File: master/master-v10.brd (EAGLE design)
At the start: 48.3 x 59.7 mm, 42 parts, among them IC2 DS3231/SO, J1 AVR_SPI_PRG_6PTH, J2 TWIG-2.0-DIPD, J3 TWIG-2.0-DIPD, J4 TWIG-2.0-DIPD, U1 MCP9804, U2 ATMEGA640/1280/2560-A, U3 FT232RL-BASICSSOP, U4 AP1117E, U5 USD-SOCKETNEW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

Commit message: agregados pads
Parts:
- added V_IN, V_OUT: MOUNT-PAD-ROUND3.0, holes:3,0-PAD
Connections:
- net VIN+: now also V_IN.B3,0
- net VIN-: now also V_OUT.B3,0
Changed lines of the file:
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@@
 <attribute name="SKU" value="PRT-09914" x="8.89" y="6.35" size="1.778" layer="27" font="vector" ratio="15" rot="R180" display="off"/>
 </element>
+<element name="V_OUT" library="holes" package="3,0-PAD" value="MOUNT-PAD-ROUND3.0" x="-124.46" y="-48.26"/>
+<element name="V_IN" library="holes" package="3,0-PAD" value="MOUNT-PAD-ROUND3.0" x="-133.35" y="-48.26"/>
 </elements>
 <signals>
@@
 <contactref element="R12" pad="2"/>
 <contactref element="U6" pad="3"/>
+<contactref element="V_IN" pad="B3,0"/>
+<wire x1="-100.65" y1="-1.3001" x2="-133.35" y2="-48.26" width="0" layer="19" extent="1-1"/>
 <wire x1="-63.37" y1="63.5" x2="-100.65" y2="-1.3001" width="0" layer="19" extent="1-1"/>
 </signal>
@@
 <contactref element="R12" pad="1"/>
 <contactref element="U6" pad="4"/>
+<contactref element="V_OUT" pad="B3,0"/>
+<wire x1="-100.65" y1="1.3001" x2="-124.46" y2="-48.26" width="0" layer="19" extent="1-1"/>
 <wire x1="-66.17" y1="63.5" x2="-100.65" y2="1.3001" width="0" layer="19" extent="1-1"/>
 </signal>

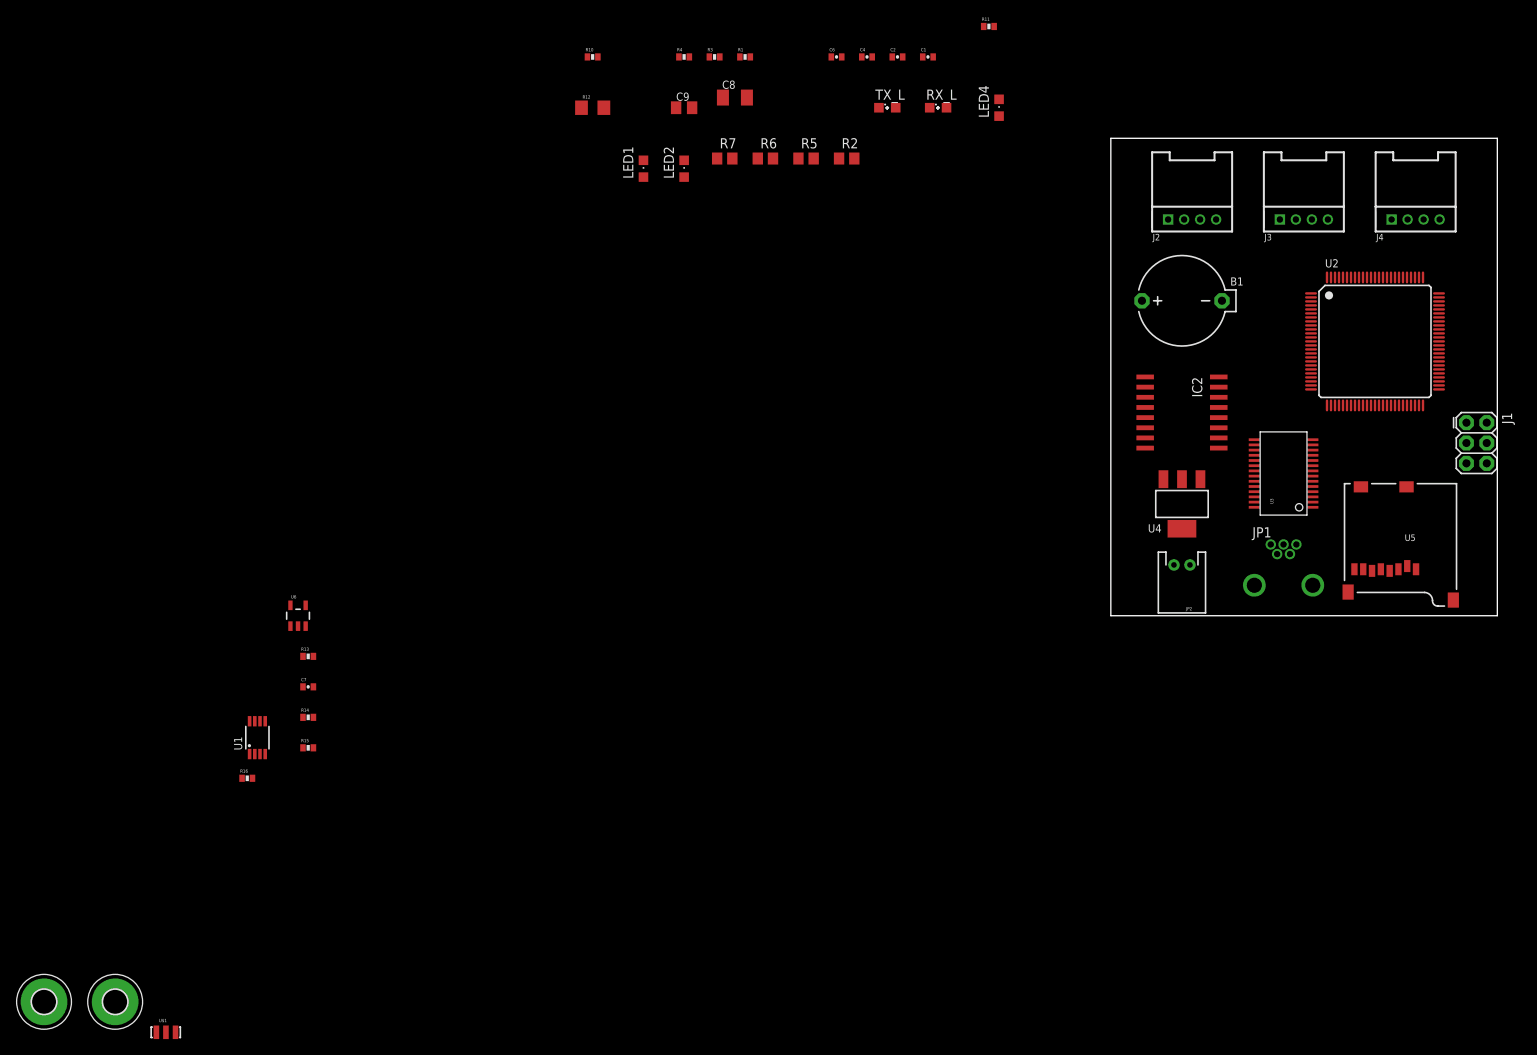
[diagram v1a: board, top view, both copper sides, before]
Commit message: actualizado brd, y arreglado tamaño de algunos componentes
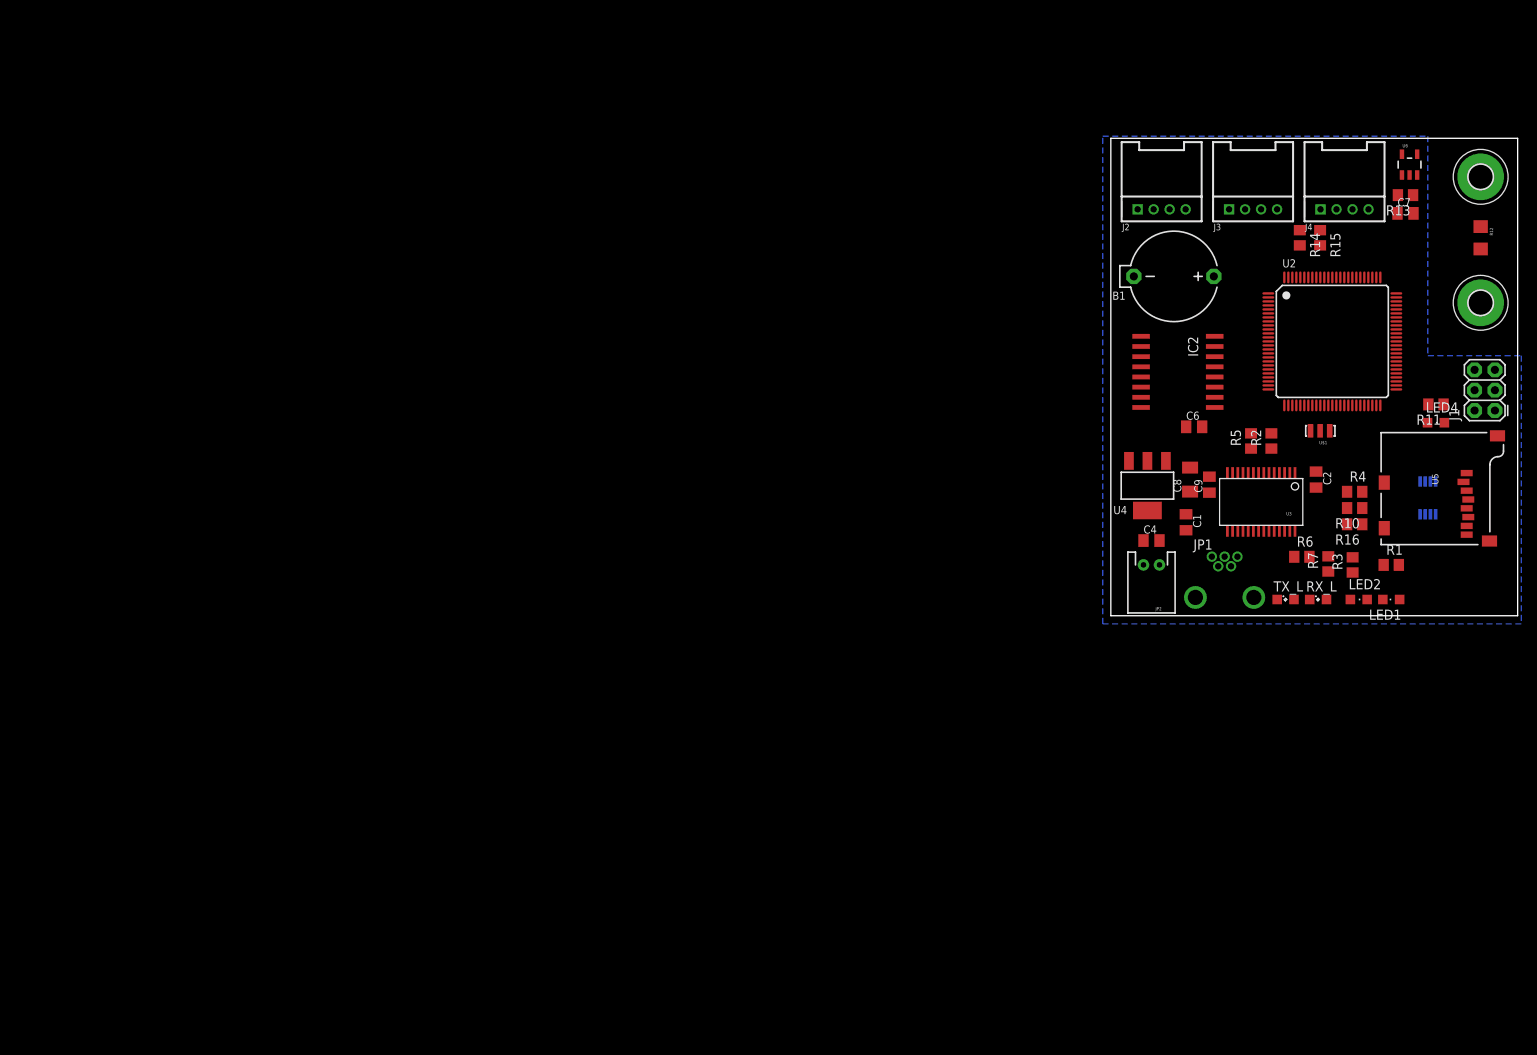
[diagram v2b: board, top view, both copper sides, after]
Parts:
- C1, C2, C4, C6, C7: device SparkFun:0402-CAP -> rcl:C0805K
- R1, R10, R11, R13, R14, R15, R16, R3, R4: device SparkFun:0402-RES -> rcl:R0805
- moved V_IN 199.7 mm to (46.2, 39.1)
- moved V_OUT 199.4 mm to (46.2, 54.9)
- moved U$1 162.7 mm to (26.2, 23.1), turned to 180 degrees
- moved U6 149.9 mm to (37.3, 56.4)
- moved C7 149.4 mm to (36.8, 50.3)
- moved U1 149.3 mm to (39.6, 14.7), flipped to the bottom
- moved R13 148.8 mm to (36.8, 52.6), turned to 180 degrees
- moved R16 142.0 mm to (30.5, 11.4), turned to 180 degrees
- moved R15 141.7 mm to (26.2, 47.2), turned to 270 degrees
- moved R14 137.7 mm to (23.6, 47.2), turned to 270 degrees
- moved R12 112.2 mm to (46.2, 47.2), turned to 270 degrees
- moved R10 110.7 mm to (30.5, 13.5), turned to 180 degrees
- moved LED1 107.9 mm to (35.1, 2.03), turned to 90 degrees
- moved R1 102.7 mm to (35.1, 6.35)
- moved R3 101.9 mm to (30.2, 6.35), turned to 90 degrees
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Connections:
- removed net N$27: U1.6
- net GND: now also U1.6
- net N$2: now also U2.34
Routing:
- added copper zone on layer 16, net GND
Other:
- board size 48.3 x 59.7 mm -> 50.9 x 59.7 mm
- board text added: "V1 1429"

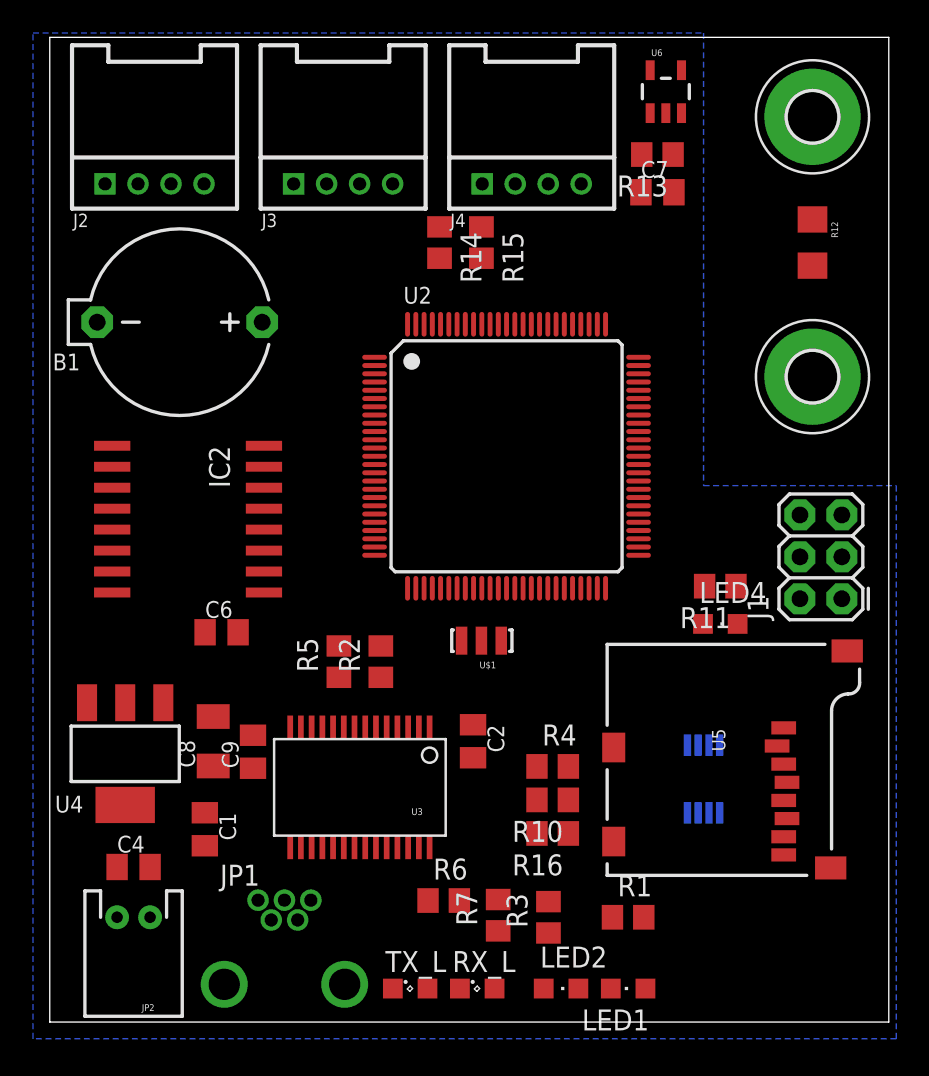
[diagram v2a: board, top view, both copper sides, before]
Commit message: orden estetico a brd + mounting holes
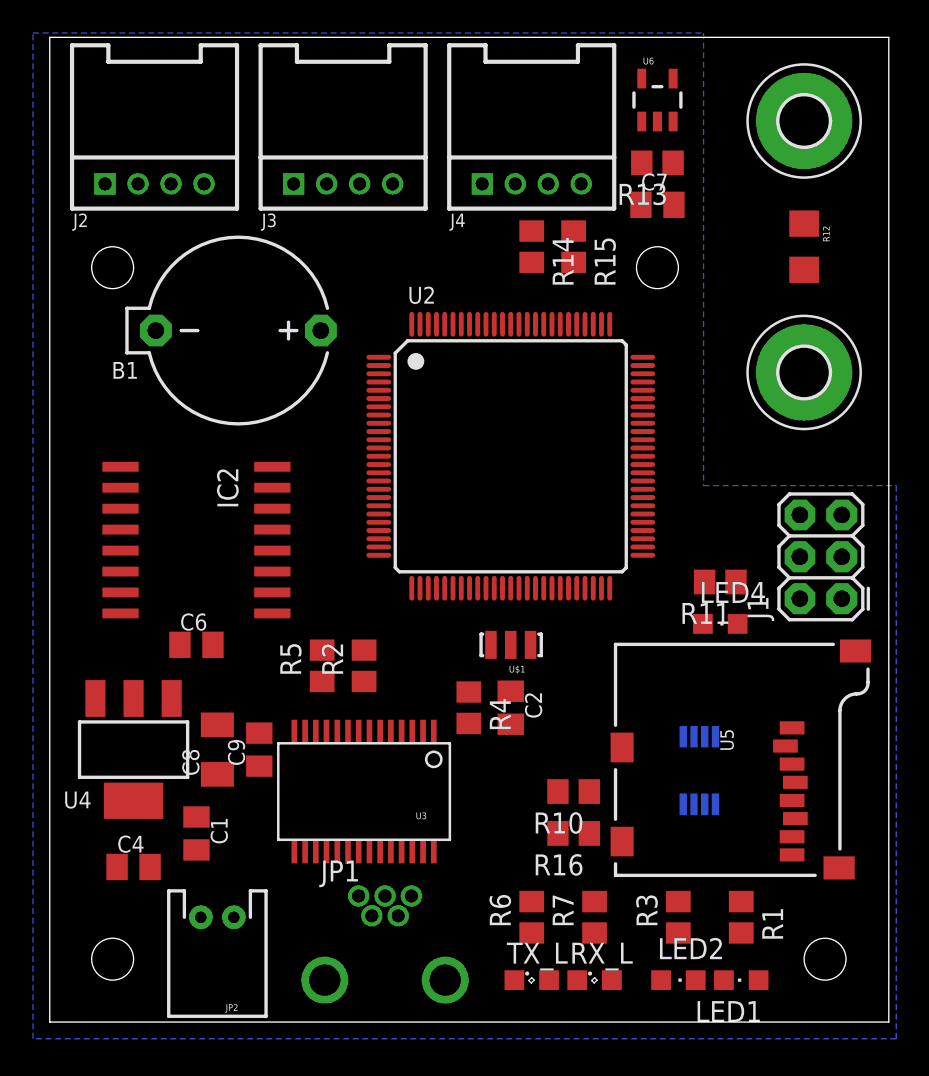
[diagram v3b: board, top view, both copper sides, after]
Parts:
- moved R3 7.87 mm to (38.1, 6.35)
- moved TX_L 7.38 mm to (29.2, 2.54)
- moved LED2 7.13 mm to (38.1, 2.54)
- moved RX_L 7.13 mm to (33.0, 2.54)
- moved LED1 6.88 mm to (41.9, 2.54)
- moved R1 6.86 mm to (41.9, 6.35), turned to 270 degrees
- moved R4 6.20 mm to (25.4, 19.1), turned to 270 degrees
- moved JP1 6.10 mm to (20.3, 2.54)
- moved R7 5.84 mm to (33.0, 6.35)
- moved R14 5.59 mm to (29.2, 47.0)
- moved R15 5.59 mm to (31.8, 47.0)
- moved R6 5.43 mm to (29.2, 6.35), turned to 90 degrees
- moved JP2 5.08 mm to (10.2, 6.35)
- moved B1 3.59 mm to (11.4, 41.9)
- moved C2 3.06 mm to (27.9, 19.1)
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
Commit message: orden en esquematico
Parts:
- moved R14 1.27 mm to (29.2, 45.7)
- moved R15 1.27 mm to (31.8, 45.7)
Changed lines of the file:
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@@
 <element name="R13" library="rcl" package="R0805" value="82k" x="36.83" y="52.07" rot="R180"/>
 <element name="C7" library="rcl" package="C0805K" value="0.1uF" x="36.83" y="49.53"/>
-<element name="R14" library="rcl" package="R0805" value="10k" x="29.21" y="46.99" rot="R270"/>
-<element name="R15" library="rcl" package="R0805" value="3.3k" x="31.75" y="46.99" rot="R270"/>
+<element name="R14" library="rcl" package="R0805" value="10k" x="29.21" y="45.72" rot="R270"/>
+<element name="R15" library="rcl" package="R0805" value="3.3k" x="31.75" y="45.72" rot="R270"/>
 <element name="U1" library="MCP9804" package="MSOP8" value="MCP9804" x="39.37" y="15.24" rot="MR0"/>
 <element name="R16" library="rcl" package="R0805" value="10k" x="31.75" y="11.43" rot="R180"/>
@@
 <wire x1="37.78" y1="52.07" x2="36.83" y2="54.5799" width="0" layer="19" extent="1-1"/>
 <wire x1="37.83" y1="49.53" x2="37.78" y2="52.07" width="0" layer="19" extent="1-1"/>
-<wire x1="31.75" y1="47.94" x2="37.83" y2="49.53" width="0" layer="19" extent="1-1"/>
-<wire x1="31.44" y1="42.29" x2="31.75" y2="47.94" width="0" layer="19" extent="1-1"/>
-<wire x1="26.21" y1="50.8" x2="31.75" y2="47.94" width="0" layer="19" extent="1-1"/>
+<wire x1="31.75" y1="46.67" x2="37.83" y2="49.53" width="0" layer="19" extent="1-1"/>
+<wire x1="31.44" y1="42.29" x2="31.75" y2="46.67" width="0" layer="19" extent="1-1"/>
+<wire x1="26.21" y1="50.8" x2="31.75" y2="46.67" width="0" layer="19" extent="1-1"/>
 <wire x1="21.975" y1="10.314" x2="21.92" y2="7.64" width="0" layer="19" extent="1-1"/>
 <wire x1="21.325" y1="10.314" x2="21.975" y2="10.314" width="0" layer="19" extent="1-1"/>
@@
 <contactref element="J3" pad="4"/>
 <contactref element="JP2" pad="2"/>
-<wire x1="20.78" y1="50.8" x2="29.21" y2="47.94" width="0" layer="19" extent="1-1"/>
+<wire x1="20.78" y1="50.8" x2="29.21" y2="46.67" width="0" layer="19" extent="1-1"/>
 <wire x1="2.7686" y1="19.6088" x2="20.78" y2="50.8" width="0" layer="19" extent="1-1"/>
 <wire x1="4.08" y1="9.398" x2="2.7686" y2="19.6088" width="0" layer="19" extent="1-1"/>
@@
 <contactref element="R14" pad="2"/>
 <contactref element="R15" pad="2"/>
-<wire x1="29.21" y1="46.04" x2="31.75" y2="46.04" width="0" layer="19" extent="1-1"/>
-<wire x1="23.94" y1="42.29" x2="29.21" y2="46.04" width="0" layer="19" extent="1-1"/>
+<wire x1="29.21" y1="44.77" x2="31.75" y2="44.77" width="0" layer="19" extent="1-1"/>
+<wire x1="23.94" y1="42.29" x2="29.21" y2="44.77" width="0" layer="19" extent="1-1"/>
 </signal>
 <signal name="CS_SD">
